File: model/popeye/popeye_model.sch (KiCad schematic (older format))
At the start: 18 parts, among them U1 74LS04, U1B1 74LS00, U1D1 74LS00, U1E1 74LS138, U1F1 74LS161, U1L1 74LS74, U2 74LS74, U2D1 74LS74, U2E1 74LS161, U2F1 74LS161, U2H1 74LS367, U2K1 74LS02, U3 74LS00, U3E1 74LS367, U3H1 74LS367, U4 74LS37, U4E1 74LS365, U6C1 74LS02

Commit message: DMA simulation ready
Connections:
- net labels removed: VB
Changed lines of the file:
@@
 Text Label 2400 7600 2    60   ~ 0
 AI
-Text Label 4200 8400 2    60   ~ 0
-VB
 Wire Wire Line
 	3100 2050 3950 2050

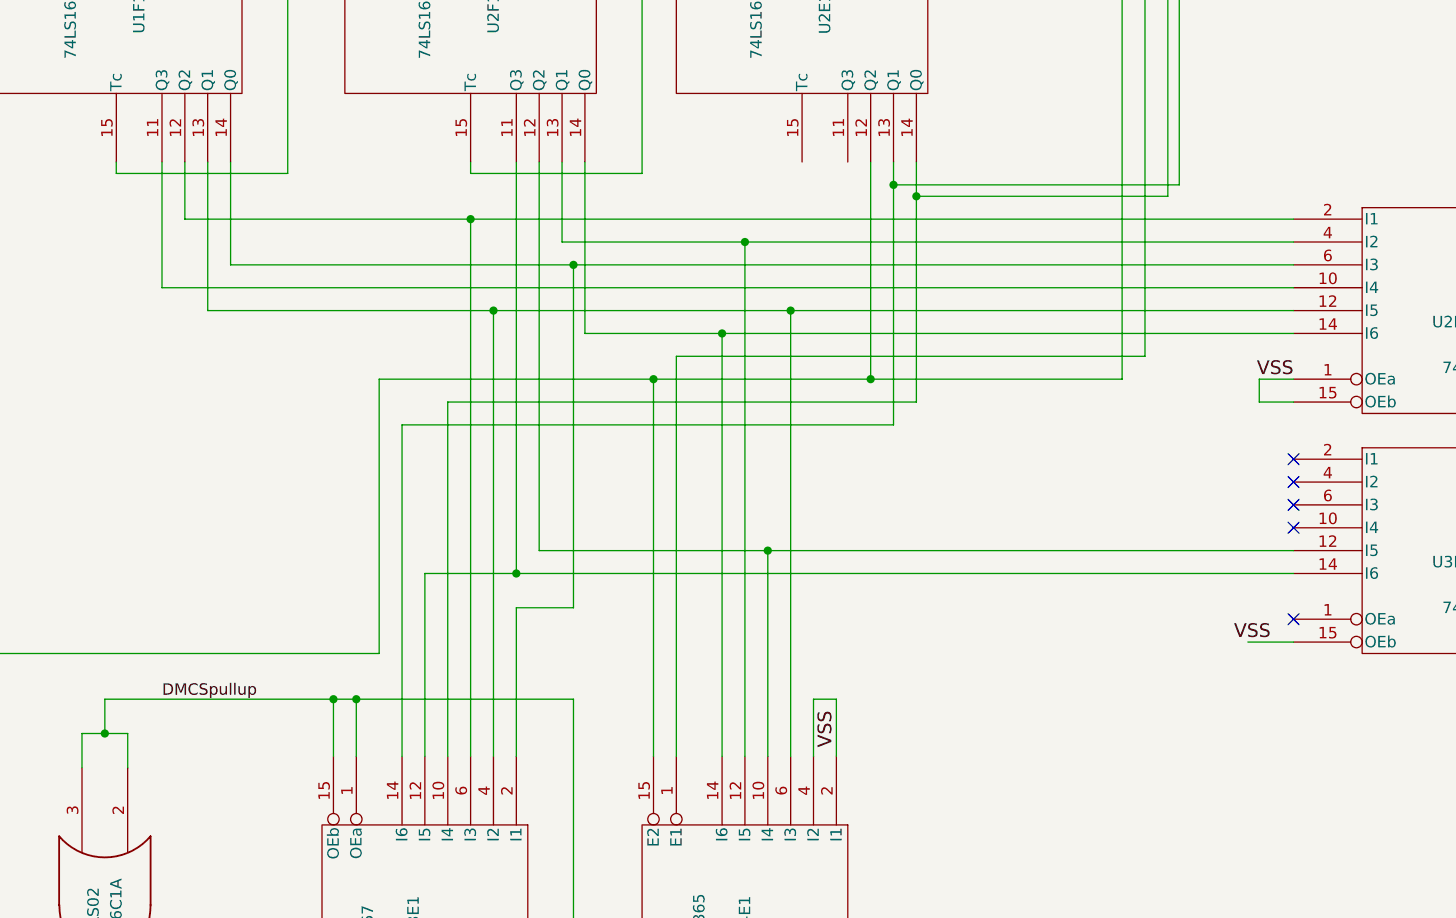
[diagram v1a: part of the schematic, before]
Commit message: Added DMA notes
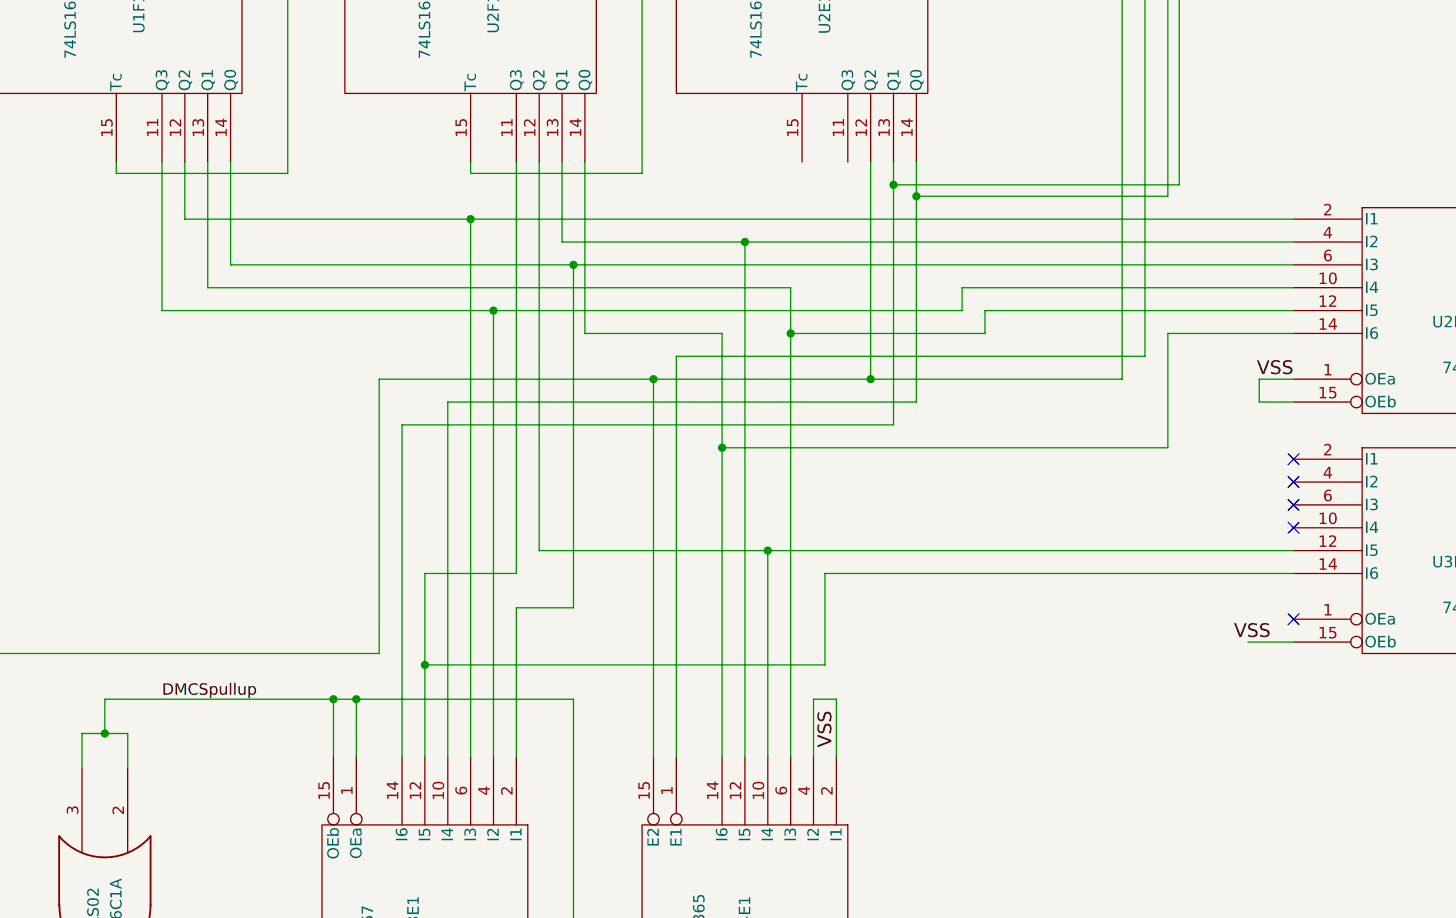
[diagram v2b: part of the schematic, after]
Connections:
- wire segments 233 -> 244
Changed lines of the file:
@@
 	14450 5200 14450 4750
-Wire Wire Line
-	19100 5300 14150 5300
-Wire Wire Line
-	14150 5300 14150 4750
-Wire Wire Line
-	19100 5400 16900 5400
-Wire Wire Line
-	14350 5400 14350 4750
-Wire Wire Line
-	19100 5500 16600 5500
 Wire Wire Line
 	16000 5500 16000 4750
@@
 	17100 7100 17100 7350
 Wire Wire Line
-	16900 7350 16900 5400
-Connection ~ 16900 5400
-Wire Wire Line
-	16600 7350 16600 5500
-Connection ~ 16600 5500
+	16600 7350 16600 6000
 Wire Wire Line
 	16700 7350 16700 5100
@@
 Wire Wire Line
 	16800 7350 16800 6450
-Connection ~ 16800 6450
-Wire Wire Line
-	15300 7350 15300 6550
-Connection ~ 15700 6550
+Wire Wire Line
+	15300 7350 15300 6950
 Wire Wire Line
 	15600 7350 15600 5400
-Connection ~ 15600 5400
 Wire Wire Line
 	15500 7350 15500 5000
@@
 	17250 5700 18350 5700
 Wire Wire Line
-	16900 5400 15600 5400
-Wire Wire Line
 	16600 5500 16000 5500
 Wire Wire Line
 	16700 5100 15900 5100
-Wire Wire Line
-	16800 6450 19100 6450
-Wire Wire Line
-	15700 6550 19100 6550
-Wire Wire Line
-	15600 5400 14350 5400
 Wire Wire Line
 	15500 5000 14250 5000
@@
 Text Label 16000 2850 0    50   ~ 0
 VDD
+Wire Wire Line
+	14150 4750 14150 5400
+Wire Wire Line
+	14150 5400 15600 5400
+Wire Wire Line
+	14350 4750 14350 5300
+Wire Wire Line
+	14350 5300 16900 5300
+Wire Wire Line
+	19100 5300 17650 5300
+Wire Wire Line
+	17650 5300 17650 5400
+Wire Wire Line
+	17650 5400 15600 5400
+Connection ~ 15600 5400
+Wire Wire Line
+	16900 5300 16900 5500
+Wire Wire Line
+	19100 5400 17750 5400
+Wire Wire Line
+	17750 5400 17750 5500
+Wire Wire Line
+	17750 5500 16900 5500
+Connection ~ 16900 5500
+Wire Wire Line
+	16900 5500 16900 7350
+Wire Wire Line
+	19100 5500 18550 5500
+Wire Wire Line
+	18550 5500 18550 6000
+Wire Wire Line
+	18550 6000 16600 6000
+Connection ~ 16600 6000
+Wire Wire Line
+	16600 6000 16600 5500
+Wire Wire Line
+	19100 6550 17050 6550
+Wire Wire Line
+	17050 6550 17050 6950
+Wire Wire Line
+	17050 6950 15300 6950
+Connection ~ 15300 6950
+Wire Wire Line
+	15300 6950 15300 6550
+Wire Wire Line
+	19100 6450 16800 6450
+Connection ~ 16800 6450
 $EndSCHEMATC

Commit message: wip
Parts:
- removed U1: 74LS04, symbol popeye_model-rescue:74LS04
- removed U1B1, U1D1, U3: 74LS00, symbol popeye_model-rescue:74LS00
- removed U1E1: 74LS138, symbol popeye_model-rescue:74LS138
- removed U1F1, U2E1, U2F1: 74LS161, symbol popeye_model-rescue:74LS161
- removed U1L1, U2, U2D1: 74LS74, symbol popeye_model-rescue:74LS74
- removed U2H1, U3E1, U3H1: 74LS367, symbol popeye_model-rescue:74LS367
- removed U2K1, U6C1: 74LS02, symbol popeye_model-rescue:74LS02
- removed U4: 74LS37, symbol popeye_model-rescue:74LS37
- removed U4E1: 74LS365, symbol popeye_model-rescue:74LS365
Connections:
- net labels removed: AD[0], AD[1], AD[2], AD[3], AD[4], AD[5], AD[6], AD[7], AD[8], AD[9], AI, AIn, BI, BIn, BUSAK, BUSAK_n, BUSRQ, BUSRQn, DMCS, DMCS0n, DMCS1n, DMCS2n, DMCS3n, DMCSpullup, DMEND, DM[0], DM[1], DM[2], DM[3], DM[4], DM[5], DM[6], DM[7], DMclr_n, HBDn, RESET, ROHVCK, ROHVS, VBn, VDD, VSS
- wire segments 244 -> 0
- no-connect marks 28 -> 0

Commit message: wip
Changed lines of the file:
@@
 $Descr A2 23386 16535
 encoding utf-8
-Sheet 1 3
+Sheet 1 4
 Title ""
 Date "2019-06-14"
@@
 F1 "video1.sch" 50
 $EndSheet
+$Sheet
+S 7500 1300 1050 850
+U 5DA6783D
+F0 "video3" 50
+F1 "video3.sch" 50
+$EndSheet
 $EndSCHEMATC

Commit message: wip
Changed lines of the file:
@@
 $Descr A4 11693 8268
 encoding utf-8
-Sheet 1 4
+Sheet 1 5
 Title ""
 Date "2019-06-14"
@@
 F1 "video3.sch" 50
 $EndSheet
+$Sheet
+S 7500 2500 1050 750
+U 5D1100BB
+F0 "video2" 50
+F1 "video2.sch" 50
+$EndSheet
 $EndSCHEMATC
